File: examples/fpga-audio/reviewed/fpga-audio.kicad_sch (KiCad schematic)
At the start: 29 parts, among them J1 3V3 IN, J2 AUDIO OUT, J3 SPI PROG, U1 iCE40UP5K, U2 PCM5102A, U3 AP2112K-1.2, U4 W25Q32JV, X1 12MHz

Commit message: Regenerate all five on the round-thirteen rules, and write the round down
The four fast boards pass their gates; measured across all five there are
zero crossings, zero doubled runs, zero mid-run width steps, every pour
piece over 8 mm2 holds its own via, and the shell reaches to 1.2 mm of
every edge. The FPGA sheet's two power blocks move clear of the frame -
the extended margin rule caught the second one this round. Its board
still fails, and the debt now has one name: four SPI nets at 11-20 mm
over plane cuts, two corners, and three detours all on the 3.3 V rail,
the twenty-link net that wants the same stated spine the 1.2 V rail got.
REVIEW.md section 18 records the round.

Co-Authored-By: Claude Fable 5 <noreply@anthropic.com>
Claude-Session: https://claude.ai/code/session_01DUj7Ltu92tWg159mCSacwY
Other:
- moved on the sheet: J1, J2

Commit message: Relieve the pads, fillet the joints, and give the board its screw holes
Three of the reviewer's manufacturing points, and they largely fall out
of the one before it - once KiCad fills the plane, the thermal relief it
was already asked for in the file actually appears.

**Thermal relief.** The zones said thermal all along; our own filler
ignored it and flooded every land solid. KiCad's does not, so every
through-hole ground pad now sits in a gap bridged by four spokes and an
iron can bring the joint up without heating a hundred square millimetres
of copper. `layout.solid_pad_connection` reports the setting when a
board turns it off: drilled pads only, because a surface pad reflows in
an oven that is heating the plane anyway and flooding it is often the
better thermal answer.

**Teardrops.** A track entering a land is a step change in width, and a
step change is where copper tears - the connector gets levered on and
off, the drill wanders, and the crack starts at the corner. `_teardrops`
replaces the first stretch of each run with a three-step taper into the
land, checked against its neighbours before it is kept, so a fillet
never eats the clearance a fine-pitch escape needs. It *replaces* rather
than overlays: laying the taper on top of the run drew the same copper
twice, and `route.acute_angle` reported all thirty of them, correctly.
`route.mixed_track_widths` learns what a fillet looks like so a properly
filleted board does not read as one nobody decided the width of.

**Mounting holes.** Four M3 holes near the corners, placed before the
router runs because they are obstacles, and slid along the edges or a
little inboard where a connector body has the corner - the motor board
and the op-amp take three, which is what those floorplans have room for.
Grounded on the motor driver, whose chassis is metal and part of the
shield, plain on the rest: bonding the enclosure to the reference is the
enclosure's decision, not the board's.

Two things that fell out of placing par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
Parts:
- added H1, H2, H3: M33, MountingHole:MountingHole_3.2mm_M3, symbol Mechanical:MountingHole
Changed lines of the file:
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@@
     (instances (project "fpga-audio" (path "/434dea94-d96f-5288-b60c-67317d440f4e" (reference "C15") (unit 1))))
+  )
+  (symbol (lib_id "Mechanical:MountingHole") (at 30.0 150.0 0.0) (unit 1)
+    (exclude_from_sim no) (in_bom yes) (on_board yes) (dnp no)
+    (property "Reference" "H1" (at 28.73 146.19 0) (effects (font (size 1.27 1.27)) (justify right)))
+    (property "Value" "M33" (at 33.81 152.54 0) (effects (font (size 1.27 1.27)) (justify left)))
+    (property "Footprint" "MountingHole:MountingHole_3.2mm_M3" (at 30.0 150.0 0) (effects (font (size 1.27 1.27)) hide))
+    (property "Datasheet" "~" (at 30.0 150.0 0) (effects (font (size 1.27 1.27)) hide))
+    (property "MPN" "n/a" (at 30.0 150.0 0) (effects (font (size 1.27 1.27)) hide))
+    (property "Manufacturer" "n/a" (at 30.0 150.0 0) (effects (font (size 1.27 1.27)) hide))
+    (instances (project "fpga-audio" (path "/434dea94-d96f-5288-b60c-67317d440f4e" (reference "H1") (unit 1))))
+  )
+  (symbol (lib_id "Mechanical:MountingHole") (at 42.7 150.0 0.0) (unit 1)
+    (exclude_from_sim no) (in_bom yes) (on_board yes) (dnp no)
+    (property "Reference" "H2" (at 41.43 146.19 0) (effects (font (size 1.27 1.27)) (justify right)))
+    (property "Value" "M33" (at 33.81 152.54 0) (effects (font (size 1.27 1.27)) (justify right)))
+    (property "Footprint" "MountingHole:MountingHole_3.2mm_M3" (at 42.7 150.0 0) (effects (font (size 1.27 1.27)) hide))
+    (property "Datasheet" "~" (at 42.7 150.0 0) (effects (font (size 1.27 1.27)) hide))
+    (property "MPN" "n/a" (at 42.7 150.0 0) (effects (font (size 1.27 1.27)) hide))
+    (property "Manufacturer" "n/a" (at 42.7 150.0 0) (effects (font (size 1.27 1.27)) hide))
+    (instances (project "fpga-audio" (path "/434dea94-d96f-5288-b60c-67317d440f4e" (reference "H2") (unit 1))))
+  )
+  (symbol (lib_id "Mechanical:MountingHole") (at 55.4 150.0 0.0) (unit 1)
+    (exclude_from_sim no) (in_bom yes) (on_board yes) (dnp no)
+    (property "Reference" "H3" (at 46.51 147.46 0) (effects (font (size 1.27 1.27)) (justify right)))
+    (property "Value" "M33" (at 46.51 152.54 0) (effects (font (size 1.27 1.27)) (justify right)))
+    (property "Footprint" "MountingHole:MountingHole_3.2mm_M3" (at 55.4 150.0 0) (effects (font (size 1.27 1.27)) hide))
+    (property "Datasheet" "~" (at 55.4 150.0 0) (effects (font (size 1.27 1.27)) hide))
+    (property "MPN" "n/a" (at 55.4 150.0 0) (effects (font (size 1.27 1.27)) hide))
+    (property "Manufacturer" "n/a" (at 55.4 150.0 0) (effects (font (size 1.27 1.27)) hide))
+    (instances (project "fpga-audio" (path "/434dea94-d96f-5288-b60c-67317d440f4e" (reference "H3") (unit 1))))
   )
   (wire (pts (xy 311.15 118.11) (xy 303.53 118.11)) (stroke (width 0) (type default)))

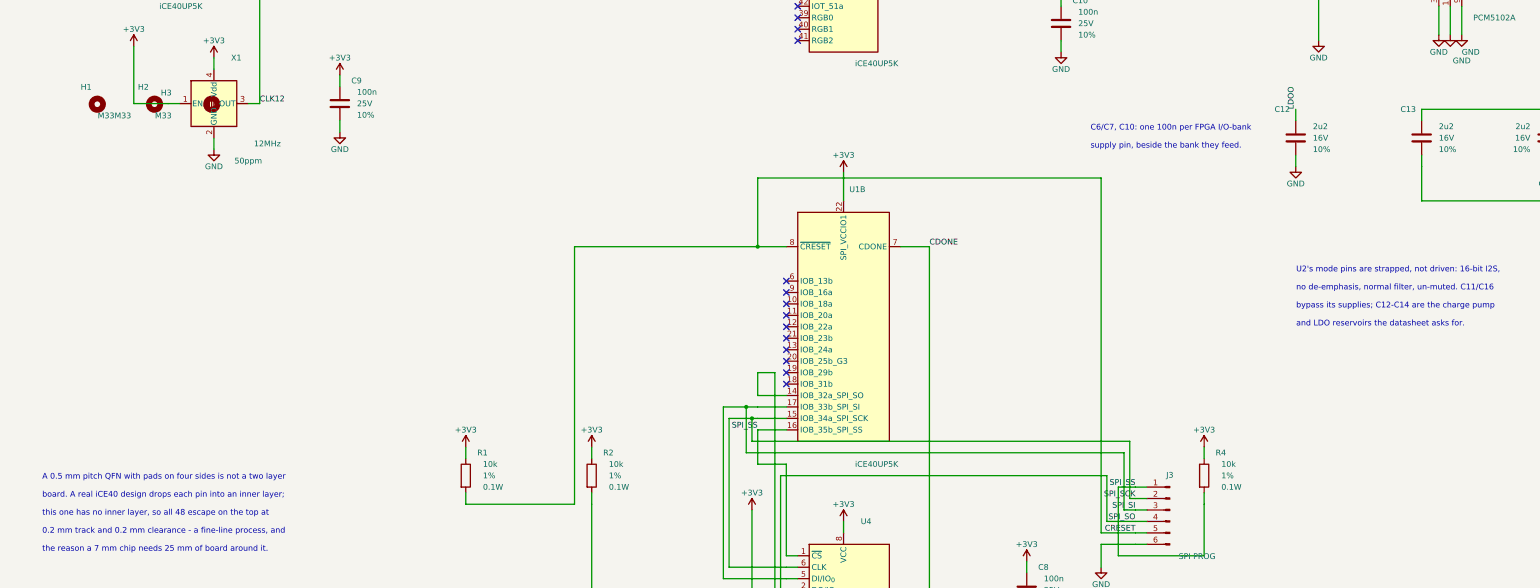
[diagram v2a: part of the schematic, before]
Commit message: Put the vias back where the copper moved, and let the fillets vote
The FPGA board came back from its re-route with two unconnected nets and
three dangling ends, and the cause was older than anything this round
added. The router hands back a via for every layer change; six passes
then reshape the copper - snapping to 45s, chamfering, spreading folds,
and now filleting - and none of them move the holes underneath. A joint
that slides a millimetre from its via is two loose ends and one broken
net, and `_unlooped` then swept the via away as orphaned, because it
kept a via only when a track ended on its exact coordinate.

Two fixes, both about what "connected" means. A via lives if kept copper
*touches* it, not if a coordinate matches. And a new `_joined` pass
re-derives the joints from the copper that actually got written: where a
net ends on two layers at one point with no via reaching it, one goes
back in. It reads the finished geometry, so it cannot drift the way six
separate passes carrying vias along with them would.

The same reasoning fixes two rules that had been measuring coordinates
rather than copper. `route.stub` matched a track end to a via's centre
exactly, and called a joint a stub whenever a reshaping pass had moved
it a quarter of a millimetre inside the very barrel it was connected to.
`route.width_step` walked a neck back to its pad and stopped at the
first width change - which, on a filleted board, is the teardrop, so
every escape's neck stopped being recognised as one.

While the three copies of the post-route pipeline were being edited for
the third time this session, they became one function. That is how
`_teardrops` had come to run on two of the three exits.

All five boards: DRC clean on both matrix versions, nothing unconnected.
Four pass their gates; the FPGA board is down to the two-layer bill it
has always had - four nets over plane cuts and one 88 degree corner.

Co-Authored-By: Claude Fable 5 <noreply@anthropic.com>
Claude-Session: https:/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
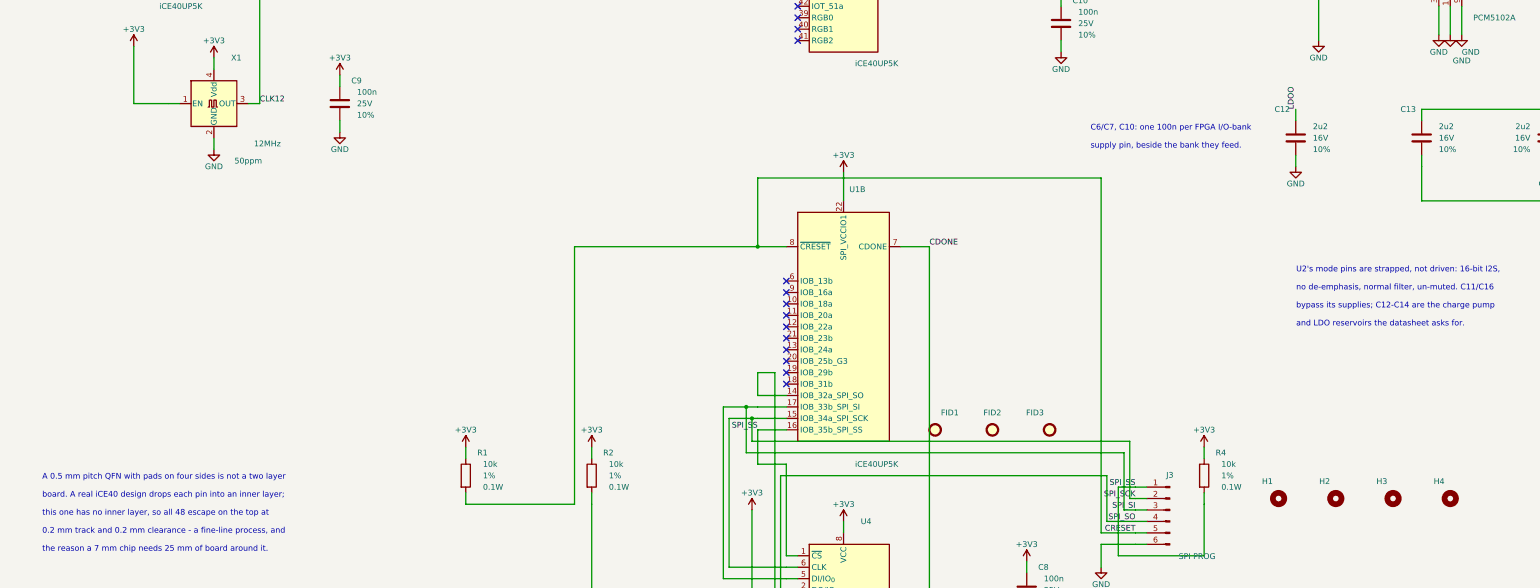
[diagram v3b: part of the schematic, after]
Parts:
- added FID1, FID2, FID3: Fiducial, Fiducial:Fiducial_1mm_Mask2mm, symbol Mechanical:Fiducial
- added H4: M3, MountingHole:MountingHole_3.2mm_M3, symbol Mechanical:MountingHole
- H1, H2, H3: value M33 -> M3; now left out of the parts list
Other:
- moved on the sheet: H1, H2, H3
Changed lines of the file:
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@@
     (instances (project "fpga-audio" (path "/434dea94-d96f-5288-b60c-67317d440f4e" (reference "C15") (unit 1))))
   )
-  (symbol (lib_id "Mechanical:MountingHole") (at 30.0 150.0 0.0) (unit 1)
-    (exclude_from_sim no) (in_bom yes) (on_board yes) (dnp no)
-    (property "Reference" "H1" (at 28.73 146.19 0) (effects (font (size 1.27 1.27)) (justify right)))
-    (property "Value" "M33" (at 33.81 152.54 0) (effects (font (size 1.27 1.27)) (justify left)))
-    (property "Footprint" "MountingHole:MountingHole_3.2mm_M3" (at 30.0 150.0 0) (effects (font (size 1.27 1.27)) hide))
-    (property "Datasheet" "~" (at 30.0 150.0 0) (effects (font (size 1.27 1.27)) hide))
-    (property "MPN" "n/a" (at 30.0 150.0 0) (effects (font (size 1.27 1.27)) hide))
-    (property "Manufacturer" "n/a" (at 30.0 150.0 0) (effects (font (size 1.27 1.27)) hide))
+  (symbol (lib_id "Mechanical:MountingHole") (at 292.1 237.49 0.0) (unit 1)
+    (exclude_from_sim no) (in_bom no) (on_board yes) (dnp no)
+    (property "Reference" "H1" (at 290.83 233.68 0) (effects (font (size 1.27 1.27)) (justify right)))
+    (property "Value" "M3" (at 295.91 240.03 0) (effects (font (size 1.27 1.27)) (justify left) hide))
+    (property "Footprint" "MountingHole:MountingHole_3.2mm_M3" (at 292.1 237.49 0) (effects (font (size 1.27 1.27)) hide))
+    (property "Datasheet" "~" (at 292.1 237.49 0) (effects (font (size 1.27 1.27)) hide))
+    (property "MPN" "n/a" (at 292.1 237.49 0) (effects (font (size 1.27 1.27)) hide))
+    (property "Manufacturer" "n/a" (at 292.1 237.49 0) (effects (font (size 1.27 1.27)) hide))
     (instances (project "fpga-audio" (path "/434dea94-d96f-5288-b60c-67317d440f4e" (reference "H1") (unit 1))))
   )
-  (symbol (lib_id "Mechanical:MountingHole") (at 42.7 150.0 0.0) (unit 1)
-    (exclude_from_sim no) (in_bom yes) (on_board yes) (dnp no)
-    (property "Reference" "H2" (at 41.43 146.19 0) (effects (font (size 1.27 1.27)) (justify right)))
-    (property "Value" "M33" (at 33.81 152.54 0) (effects (font (size 1.27 1.27)) (justify right)))
-    (property "Footprint" "MountingHole:MountingHole_3.2mm_M3" (at 42.7 150.0 0) (effects (font (size 1.27 1.27)) hide))
-    (property "Datasheet" "~" (at 42.7 150.0 0) (effects (font (size 1.27 1.27)) hide))
-    (property "MPN" "n/a" (at 42.7 150.0 0) (effects (font (size 1.27 1.27)) hide))
-    (property "Manufacturer" "n/a" (at 42.7 150.0 0) (effects (font (size 1.27 1.27)) hide))
+  (symbol (lib_id "Mechanical:MountingHole") (at 304.8 237.49 0.0) (unit 1)
+    (exclude_from_sim no) (in_bom no) (on_board yes) (dnp no)
+    (property "Reference" "H2" (at 303.53 233.68 0) (effects (font (size 1.27 1.27)) (justify right)))
+    (property "Value" "M3" (at 308.61 240.03 0) (effects (font (size 1.27 1.27)) (justify left) hide))
+    (property "Footprint" "MountingHole:MountingHole_3.2mm_M3" (at 304.8 237.49 0) (effects (font (size 1.27 1.27)) hide))
+    (property "Datasheet" "~" (at 304.8 237.49 0) (effects (font (size 1.27 1.27)) hide))
+    (property "MPN" "n/a" (at 304.8 237.49 0) (effects (font (size 1.27 1.27)) hide))
+    (property "Manufacturer" "n/a" (at 304.8 237.49 0) (effects (font (size 1.27 1.27)) hide))
     (instances (project "fpga-audio" (path "/434dea94-d96f-5288-b60c-67317d440f4e" (reference "H2") (unit 1))))
   )
-  (symbol (lib_id "Mechanical:MountingHole") (at 55.4 150.0 0.0) (unit 1)
-    (exclude_from_sim no) (in_bom yes) (on_board yes) (dnp no)
-    (property "Reference" "H3" (at 46.51 147.46 0) (effects (font (size 1.27 1.27)) (justify right)))
-    (property "Value" "M33" (at 46.51 152.54 0) (effects (font (size 1.27 1.27)) (justify right)))
-    (property "Footprint" "MountingHole:MountingHole_3.2mm_M3" (at 55.4 150.0 0) (effects (font (size 1.27 1.27)) hide))
-    (property "Datasheet" "~" (at 55.4 150.0 0) (effects (font (size 1.27 1.27)) hide))
-    (property "MPN" "n/a" (at 55.4 150.0 0) (effects (font (size 1.27 1.27)) hide))
-    (property "Manufacturer" "n/a" (at 55.4 150.0 0) (effects (font (size 1.27 1.27)) hide))
+  (symbol (lib_id "Mechanical:MountingHole") (at 317.5 237.49 0.0) (unit 1)
+    (exclude_from_sim no) (in_bom no) (on_board yes) (dnp no)
+    (property "Reference" "H3" (at 316.23 233.68 0) (effects (font (size 1.27 1.27)) (justify right)))
+    (property "Value" "M3" (at 321.31 240.03 0) (effects (font (size 1.27 1.27)) (justify left) hide))
+    (property "Footprint" "MountingHole:MountingHole_3.2mm_M3" (at 317.5 237.49 0) (effects (font (size 1.27 1.27)) hide))
+    (property "Datasheet" "~" (at 317.5 237.49 0) (effects (font (size 1.27 1.27)) hide))
+    (property "MPN" "n/a" (at 317.5 237.49 0) (effects (font (size 1.27 1.27)) hide))
+    (property "Manufacturer" "n/a" (at 317.5 237.49 0) (effects (font (size 1.27 1.27)) hide))
     (instances (project "fpga-audio" (path "/434dea94-d96f-5288-b60c-67317d440f4e" (reference "H3") (unit 1))))
   )
+  (symbol (lib_id "Mechanical:MountingHole") (at 330.20000000000005 237.49 0.0) (unit 1)
+    (exclude_from_sim no) (in_bom no) (on_board yes) (dnp no)
+    (property "Reference" "H4" (at 328.93 233.68 0) (effects (font (size 1.27 1.27)) (justify right)))
+    (property "Value" "M3" (at 334.01 240.03 0) (effects (font (size 1.27 1.27)) (justify left) hide))
+    (property "Footprint" "MountingHole:MountingHole_3.2mm_M3" (at 330.20000000000005 237.49 0) (effects (font (size 1.27 1.27)) hide))
+    (property "Datasheet" "~" (at 330.20000000000005 237.49 0) (effects (font (size 1.27 1.27)) hide))
+    (property "MPN" "n/a" (at 330.20000000000005 237.49 0) (effects (font (size 1.27 1.27)) hide))
+    (property "Manufacturer" "n/a" (at 330.20000000000005 237.49 0) (effects (font (size 1.27 1.27)) hide))
+    (instances (project "fpga-audio" (path "/434dea94-d96f-5288-b60c-67317d440f4e" (reference "H4") (unit 1))))
+  )
+  (symbol (lib_id "Mechanical:Fiducial") (at 215.9 222.25 0.0) (unit 1)
+    (exclude_from_sim no) (in_bom no) (on_board yes) (dnp no)
+    (property "Reference" "FID1" (at 217.17 218.44 0) (effects (font (size 1.27 1.27)) (justify left)))
+    (property "Value" "Fiducial" (at 217.17 229.87 0) (effects (font (size 1.27 1.27)) (justify left) hide))
+    (property "Footprint" "Fiducial:Fiducial_1mm_Mask2mm" (at 215.9 222.25 0) (effects (font (size 1.27 1.27)) hide))
+    (property "Datasheet" "~" (at 215.9 222.25 0) (effects (font (size 1.27 1.27)) hide))
+    (property "MPN" "n/a" (at 215.9 222.25 0) (effects (font (size 1.27 1.27)) hide))
+    (property "Manufacturer" "n/a" (at 215.9 222.25 0) (effects (font (size 1.27 1.27)) hide))
+    (instances (project "fpga-audio" (path "/434dea94-d96f-5288-b60c-67317d440f4e" (reference "FID1") (unit 1))))
+  )
+  (symbol (lib_id "Mechanical:Fiducial") (at 228.6 222.25 0.0) (unit 1)
+    (exclude_from_sim no) (in_bom no) (on_board yes) (dnp no)
+    (property "Reference" "FID2" (at 228.6 218.44 0) (effects (font (size 1.27 1.27))))
+    (property "Value" "Fiducial" (at 229.87 229.87 0) (effects (font (size 1.27 1.27)) (justify left) hide))
+    (property "Footprint" "Fiducial:Fiducial_1mm_Mask2mm" (at 228.6 222.25 0) (effects (font (size 1.27 1.27)) hide))
+    (property "Datasheet" "~" (at 228.6 222.25 0) (effects (font (size 1.27 1.27)) hide))
+    (property "MPN" "n/a" (at 228.6 222.25 0) (effects (font (size 1.27 1.27)) hide))
+    (property "Manufacturer" "n/a" (at 228.6 222.25 0) (effects (font (size 1.27 1.27)) hide))
+    (instances (project "fpga-audio" (path "/434dea94-d96f-5288-b60c-67317d440f4e" (reference "FID2") (unit 1))))
+  )
+  (symbol (lib_id "Mechanical:Fiducial") (at 241.3 222.25 0.0) (unit 1)
+    (exclude_from_sim no) (in_bom no) (on_board yes) (dnp no)
+    (property "Reference" "FID3" (at 240.03 218.44 0) (effects (font (size 1.27 1.27)) (justify right)))
+    (property "Value" "Fiducial" (at 237.49 224.79 0) (effects (font (size 1.27 1.27)) (justify right) hide))
+    (property "Footprint" "Fiducial:Fiducial_1mm_Mask2mm" (at 241.3 222.25 0) (effects (font (size 1.27 1.27)) hide))
+    (property "Datasheet" "~" (at 241.3 222.25 0) (effects (font (size 1.27 1.27)) hide))
+    (property "MPN" "n/a" (at 241.3 222.25 0) (effects (font (size 1.27 1.27)) hide))
+    (property "Manufacturer" "n/a" (at 241.3 222.25 0) (effects (font (size 1.27 1.27)) hide))
+    (instances (project "fpga-audio" (path "/434dea94-d96f-5288-b60c-67317d440f4e" (reference "FID3") (unit 1))))
+  )
   (wire (pts (xy 311.15 118.11) (xy 303.53 118.11)) (stroke (width 0) (type default)))
